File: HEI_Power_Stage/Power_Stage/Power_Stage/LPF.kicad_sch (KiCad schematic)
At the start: 2 parts

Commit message: spi isolation
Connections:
- net GNDPWR renamed HV-
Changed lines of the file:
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@@
 			)
 		)
-		(property "Value" "GNDPWR"
+		(property "Value" "HV-"
 			(at 137.16 95.25 0)
 			(effects

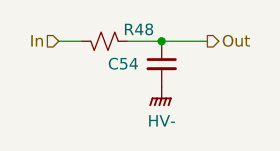
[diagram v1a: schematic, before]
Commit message: new gate driver
added new gate drivers, changes sensing to be non isolated, removed adcs on gate drive pages, added connector, added dc link cap, need to still change isolation page to just be iso amp, need to adjust power input and sensing for hv bus
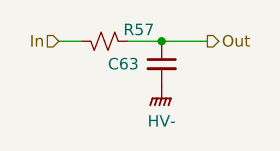
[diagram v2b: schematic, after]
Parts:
- renumbered C54 to C63, R48 to R57
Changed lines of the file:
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@@
 		(on_board yes)
 		(dnp no)
-		(property "Reference" "R48"
+		(property "Reference" "R57"
 			(at 134.62 85.09 90)
 			(effects
@@
 		(instances
 			(project "Power_Stage"
-				(path "/4073579f-dff4-4919-be9b-9c43467e22c1/fdb1cb22-51b8-420c-a9c7-ed601f391b52/b3aa0955-8146-4e7d-bc37-12b2532dd7f7"
-					(reference "R48")
-					(unit 1)
-				)
-				(path "/4073579f-dff4-4919-be9b-9c43467e22c1/d06aea5d-6634-499e-bc84-2b0ee963ac5c/b3aa0955-8146-4e7d-bc37-12b2532dd7f7"
-					(reference "R49")
-					(unit 1)
-				)
-				(path "/4073579f-dff4-4919-be9b-9c43467e22c1/fc0c4d71-751a-405d-a2b0-dee4001cda35/b3aa0955-8146-4e7d-bc37-12b2532dd7f7"
-					(reference "R50")
-					(unit 1)
-				)
 				(path "/4073579f-dff4-4919-be9b-9c43467e22c1/4b4528f4-b188-451e-92e0-694bcc5262fb"
 					(reference "R57")
@@
 		(on_board yes)
 		(dnp no)
-		(property "Reference" "#PWR056"
+		(property "Reference" "#PWR068"
 			(at 137.16 96.52 0)
 			(effects
@@
 		(instances
 			(project "Power_Stage"
-				(path "/4073579f-dff4-4919-be9b-9c43467e22c1/fdb1cb22-51b8-420c-a9c7-ed601f391b52/b3aa0955-8146-4e7d-bc37-12b2532dd7f7"
-					(reference "#PWR056")
-					(unit 1)
-				)
-				(path "/4073579f-dff4-4919-be9b-9c43467e22c1/d06aea5d-6634-499e-bc84-2b0ee963ac5c/b3aa0955-8146-4e7d-bc37-12b2532dd7f7"
-					(reference "#PWR057")
-					(unit 1)
-				)
-				(path "/4073579f-dff4-4919-be9b-9c43467e22c1/fc0c4d71-751a-405d-a2b0-dee4001cda35/b3aa0955-8146-4e7d-bc37-12b2532dd7f7"
-					(reference "#PWR058")
-					(unit 1)
-				)
 				(path "/4073579f-dff4-4919-be9b-9c43467e22c1/4b4528f4-b188-451e-92e0-694bcc5262fb"
 					(reference "#PWR068")
@@
 		(on_board yes)
 		(dnp no)
-		(property "Reference" "C54"
+		(property "Reference" "C63"
 			(at 134.62 88.9 0)
 			(effects
@@
 		(instances
 			(project "Power_Stage"
-				(path "/4073579f-dff4-4919-be9b-9c43467e22c1/fdb1cb22-51b8-420c-a9c7-ed601f391b52/b3aa0955-8146-4e7d-bc37-12b2532dd7f7"
-					(reference "C54")
-					(unit 1)
-				)
-				(path "/4073579f-dff4-4919-be9b-9c43467e22c1/d06aea5d-6634-499e-bc84-2b0ee963ac5c/b3aa0955-8146-4e7d-bc37-12b2532dd7f7"
-					(reference "C55")
-					(unit 1)
-				)
-				(path "/4073579f-dff4-4919-be9b-9c43467e22c1/fc0c4d71-751a-405d-a2b0-dee4001cda35/b3aa0955-8146-4e7d-bc37-12b2532dd7f7"
-					(reference "C56")
-					(unit 1)
-				)
 				(path "/4073579f-dff4-4919-be9b-9c43467e22c1/4b4528f4-b188-451e-92e0-694bcc5262fb"
 					(reference "C63")
